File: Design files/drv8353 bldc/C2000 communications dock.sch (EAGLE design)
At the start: 25 parts, among them IC1 ADUM1411ARWZ, J1 B03B-HCMKS, J3 SS-6488-NF-A431, U1 3352T-1-203LF

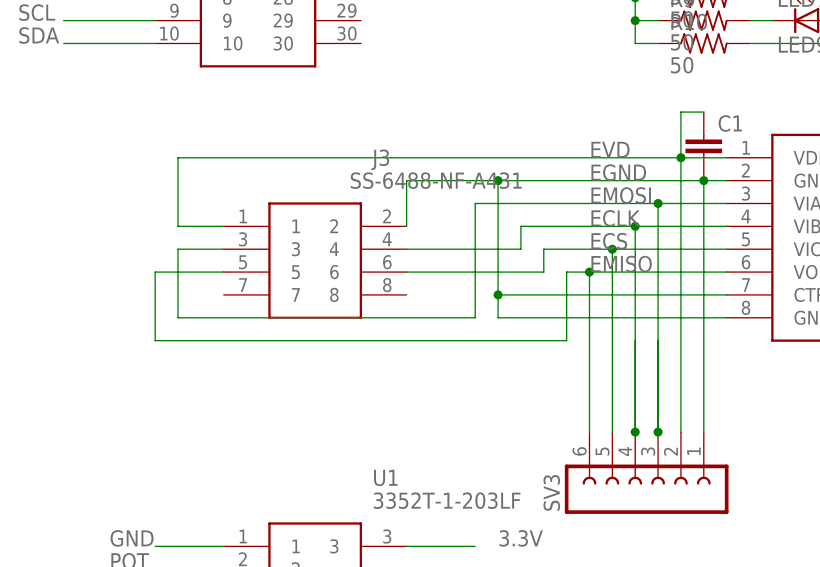
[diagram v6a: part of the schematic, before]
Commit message: reroute to match aux
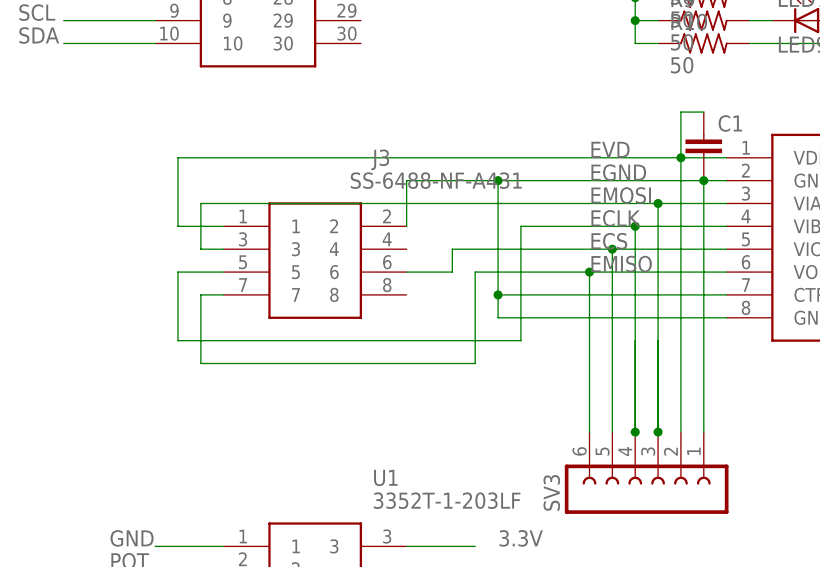
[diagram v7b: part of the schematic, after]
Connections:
- net ECLK: now also J3.5; no longer J3.4
- net EMISO: now also J3.7; no longer J3.5
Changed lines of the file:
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@@
 <pinref part="IC1" gate="G$1" pin="VDD1"/>
 <wire x1="-2.54" y1="25.4" x2="53.34" y2="25.4" width="0.1524" layer="91"/>
-<pinref part="J3" gate="G$1" pin="1"/>
 <wire x1="53.34" y1="25.4" x2="58.42" y2="25.4" width="0.1524" layer="91"/>
-<wire x1="2.54" y1="17.78" x2="-2.54" y2="17.78" width="0.1524" layer="91"/>
-<wire x1="-2.54" y1="17.78" x2="-2.54" y2="25.4" width="0.1524" layer="91"/>
 <pinref part="C1" gate="G$1" pin="1"/>
 <wire x1="55.88" y1="30.48" x2="53.34" y2="30.48" width="0.1524" layer="91"/>
@@
 <pinref part="SV3" gate="G$1" pin="2"/>
 <wire x1="53.34" y1="25.4" x2="53.34" y2="-5.08" width="0.1524" layer="91"/>
+<pinref part="J3" gate="G$1" pin="1"/>
+<wire x1="2.54" y1="17.78" x2="-2.54" y2="17.78" width="0.1524" layer="91"/>
+<wire x1="-2.54" y1="17.78" x2="-2.54" y2="25.4" width="0.1524" layer="91"/>
 </segment>
 </net>
@@
 <segment>
 <pinref part="IC1" gate="G$1" pin="VIB"/>
-<pinref part="J3" gate="G$1" pin="4"/>
-<wire x1="22.86" y1="15.24" x2="35.56" y2="15.24" width="0.1524" layer="91"/>
-<wire x1="35.56" y1="15.24" x2="35.56" y2="17.78" width="0.1524" layer="91"/>
 <wire x1="35.56" y1="17.78" x2="48.26" y2="17.78" width="0.1524" layer="91"/>
 <wire x1="48.26" y1="17.78" x2="58.42" y2="17.78" width="0.1524" layer="91"/>
@@
 <junction x="48.26" y="-5.08"/>
 <wire x1="48.26" y1="-5.08" x2="48.26" y2="5.08" width="0.1524" layer="91"/>
+<wire x1="35.56" y1="17.78" x2="35.56" y2="5.08" width="0.1524" layer="91"/>
+<wire x1="35.56" y1="5.08" x2="-2.54" y2="5.08" width="0.1524" layer="91"/>
+<wire x1="-2.54" y1="5.08" x2="-2.54" y2="12.7" width="0.1524" layer="91"/>
+<pinref part="J3" gate="G$1" pin="5"/>
+<wire x1="-2.54" y1="12.7" x2="2.54" y2="12.7" width="0.1524" layer="91"/>
 </segment>
 </net>
 <net name="EMISO" class="0">
 <segment>
-<pinref part="J3" gate="G$1" pin="5"/>
-<wire x1="2.54" y1="12.7" x2="-5.08" y2="12.7" width="0.1524" layer="91"/>
-<wire x1="-5.08" y1="12.7" x2="-5.08" y2="5.08" width="0.1524" layer="91"/>
-<wire x1="-5.08" y1="5.08" x2="40.64" y2="5.08" width="0.1524" layer="91"/>
-<wire x1="40.64" y1="5.08" x2="40.64" y2="12.7" width="0.1524" layer="91"/>
 <label x="43.18" y="12.7" size="1.778" layer="95"/>
 <pinref part="IC1" gate="G$1" pin="VOD"/>
 <wire x1="58.42" y1="12.7" x2="43.18" y2="12.7" width="0.1524" layer="91"/>
 <pinref part="SV3" gate="G$1" pin="6"/>
-<wire x1="43.18" y1="12.7" x2="40.64" y2="12.7" width="0.1524" layer="91"/>
 <junction x="43.18" y="12.7"/>
 <wire x1="43.18" y1="-5.08" x2="43.18" y2="12.7" width="0.1524" layer="91"/>
+<wire x1="43.18" y1="12.7" x2="30.48" y2="12.7" width="0.1524" layer="91"/>
+<wire x1="30.48" y1="12.7" x2="30.48" y2="2.54" width="0.1524" layer="91"/>
+<wire x1="30.48" y1="2.54" x2="0" y2="2.54" width="0.1524" layer="91"/>
+<wire x1="0" y1="2.54" x2="0" y2="10.16" width="0.1524" layer="91"/>
+<pinref part="J3" gate="G$1" pin="7"/>
+<wire x1="0" y1="10.16" x2="2.54" y2="10.16" width="0.1524" layer="91"/>
 </segment>
 </net>
@@
 <net name="EMOSI" class="0">
 <segment>
-<pinref part="J3" gate="G$1" pin="3"/>
-<wire x1="2.54" y1="15.24" x2="-2.54" y2="15.24" width="0.1524" layer="91"/>
-<wire x1="-2.54" y1="15.24" x2="-2.54" y2="7.62" width="0.1524" layer="91"/>
-<wire x1="-2.54" y1="7.62" x2="30.48" y2="7.62" width="0.1524" layer="91"/>
-<wire x1="30.48" y1="7.62" x2="30.48" y2="20.32" width="0.1524" layer="91"/>
 <pinref part="IC1" gate="G$1" pin="VIA"/>
 <wire x1="58.42" y1="20.32" x2="50.8" y2="20.32" width="0.1524" layer="91"/>
-<wire x1="30.48" y1="20.32" x2="50.8" y2="20.32" width="0.1524" layer="91"/>
 <wire x1="50.8" y1="-5.08" x2="50.8" y2="20.32" width="0.1524" layer="91"/>
 <junction x="50.8" y="20.32"/>
@@
 <junction x="50.8" y="-5.08"/>
 <wire x1="50.8" y1="-5.08" x2="50.8" y2="5.08" width="0.1524" layer="91"/>
+<wire x1="50.8" y1="20.32" x2="0" y2="20.32" width="0.1524" layer="91"/>
+<wire x1="0" y1="20.32" x2="0" y2="15.24" width="0.1524" layer="91"/>
+<pinref part="J3" gate="G$1" pin="3"/>
+<wire x1="0" y1="15.24" x2="2.54" y2="15.24" width="0.1524" layer="91"/>
 </segment>
 </net>
@@
 <pinref part="IC1" gate="G$1" pin="VIC"/>
 <wire x1="58.42" y1="15.24" x2="45.72" y2="15.24" width="0.1524" layer="91"/>
-<wire x1="45.72" y1="15.24" x2="38.1" y2="15.24" width="0.1524" layer="91"/>
-<wire x1="38.1" y1="15.24" x2="38.1" y2="12.7" width="0.1524" layer="91"/>
-<pinref part="J3" gate="G$1" pin="6"/>
-<wire x1="38.1" y1="12.7" x2="22.86" y2="12.7" width="0.1524" layer="91"/>
 <label x="43.18" y="15.24" size="1.778" layer="95"/>
 <pinref part="SV3" gate="G$1" pin="5"/>
 <wire x1="45.72" y1="-5.08" x2="45.72" y2="15.24" width="0.1524" layer="91"/>
 <junction x="45.72" y="15.24"/>
-</segment>
-</net>
+<pinref part="J3" gate="G$1" pin="6"/>
+<wire x1="22.86" y1="12.7" x2="27.94" y2="12.7" width="0.1524" layer="91"/>
+<wire x1="27.94" y1="12.7" x2="27.94" y2="15.24" width="0.1524" layer="91"/>
+<wire x1="27.94" y1="15.24" x2="45.72" y2="15.24" width="0.1524" layer="91"/>
+</segment>
+</net>
